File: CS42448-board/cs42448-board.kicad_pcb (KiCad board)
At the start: 2 copper layers, 114.2 x 58.7 mm, 134 parts, among them J1 Channel IN 1-2, J10 Channel OUT 7-8, J2 Channel IN 3-4, J3 Channel IN 5-6, J4 PMOD_DAC_IN, J5 PMOD_ADC_OUT, J6 Conn_Input, J7 Channel OUT 1-2, J8 Channel OUT 3-4, J9 Channel OUT 5-6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

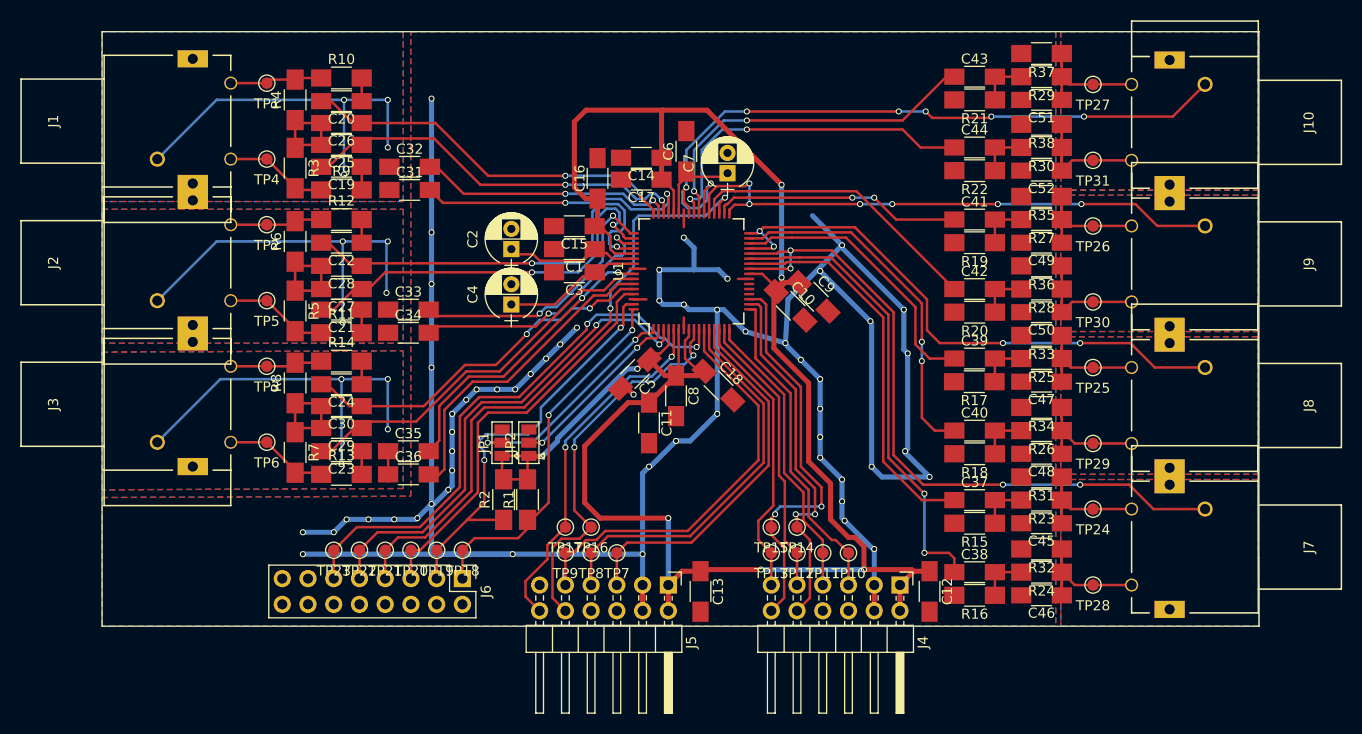
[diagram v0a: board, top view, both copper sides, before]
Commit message: Fix silkscreen
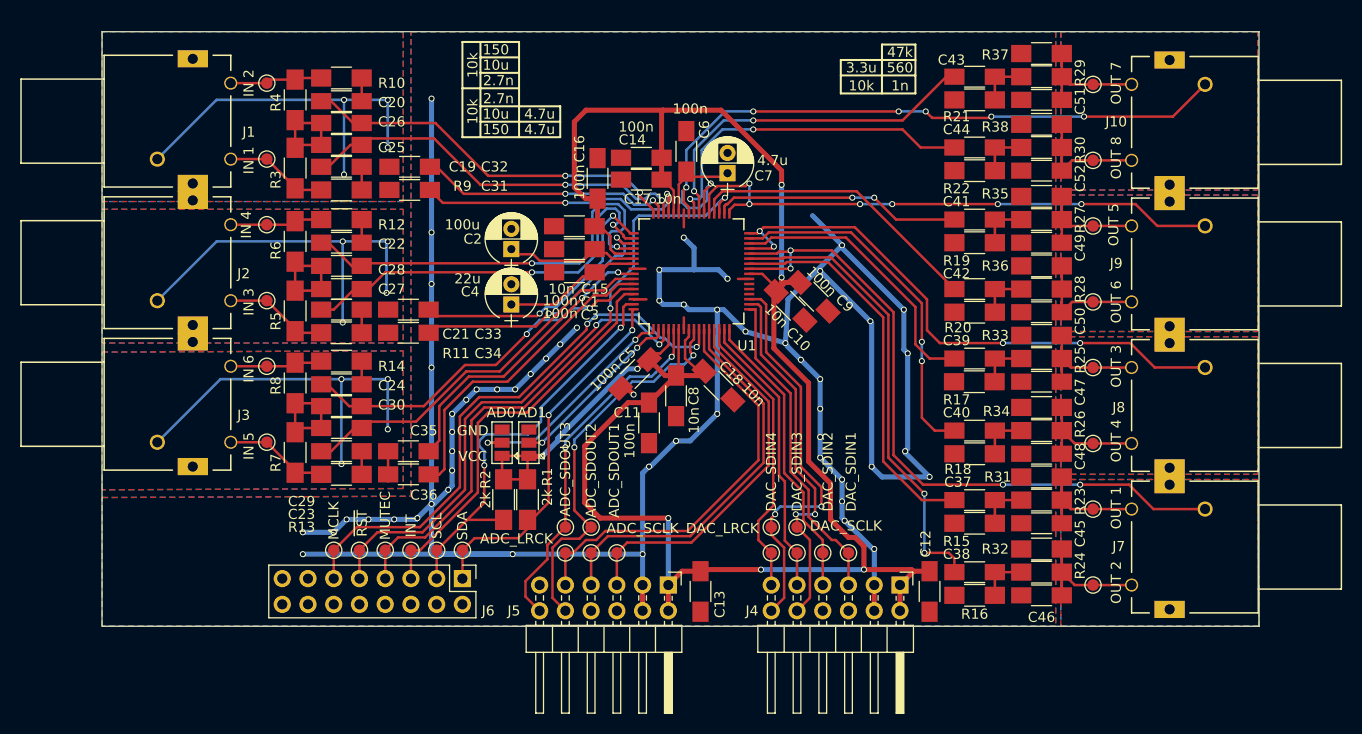
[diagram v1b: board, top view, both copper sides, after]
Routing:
- net +3V3: track 214.8 -> 215.6 mm
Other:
- board text added: "GND"
- board text added: "VCC"

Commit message: Update to rev2: fix RCA footprint
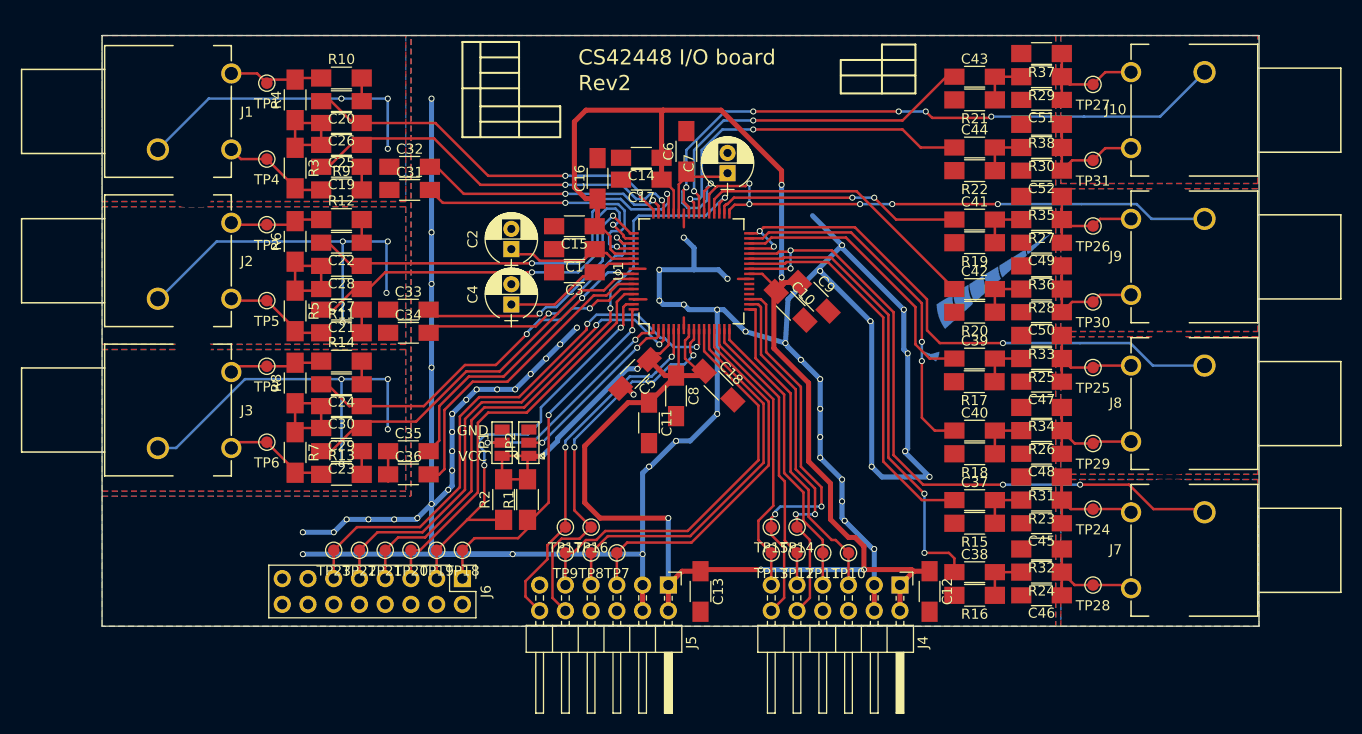
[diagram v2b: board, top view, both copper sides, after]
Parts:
- added G***: LOGO, Logos:Logos, B.Cu at (180.7, 119.1)
- moved J10 1.20 mm to (218.2, 90.3)
- moved J1 0.96 mm to (104.4, 90.4)
- moved J9 0.70 mm to (218.2, 104.8)
- moved J3 0.57 mm to (104.4, 119.9)
- moved J7 0.33 mm to (218.2, 133.7)
- moved J2 0.20 mm to (104.4, 105.2)
- moved J8 0.19 mm to (218.2, 119.3)
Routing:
- net /ADC input filter/Channel_1-2_Com: track 47.5 -> 40.0 mm, vias 4 -> 3
- net /DAC output filter/Channel_7-: track 70.7 -> 71.1 mm, vias 7 -> 6
- net /DAC output filter/Channel_5-: track 56.8 -> 56.4 mm, vias 6 -> 5
- net /DAC output filter/Channel_3-: track 57.4 -> 57.2 mm, vias 4 -> 3
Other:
- board size 114.2 x 58.7 mm -> 114.2 x 58.3 mm
- board text added: "CS42448 I/O board"
- board text added: "Rev2"

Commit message: Change logo name in library
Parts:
- G***: footprint Logos:Logos -> Logos:Unicorn_old
